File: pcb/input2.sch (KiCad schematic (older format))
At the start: 33 parts, among them U4 PCEngineExpansion, U5 FS7140-01G-XTD, U6 PCM1808PWR, U7 SI5351C-B, U8 74153, Y1 25.000MHz

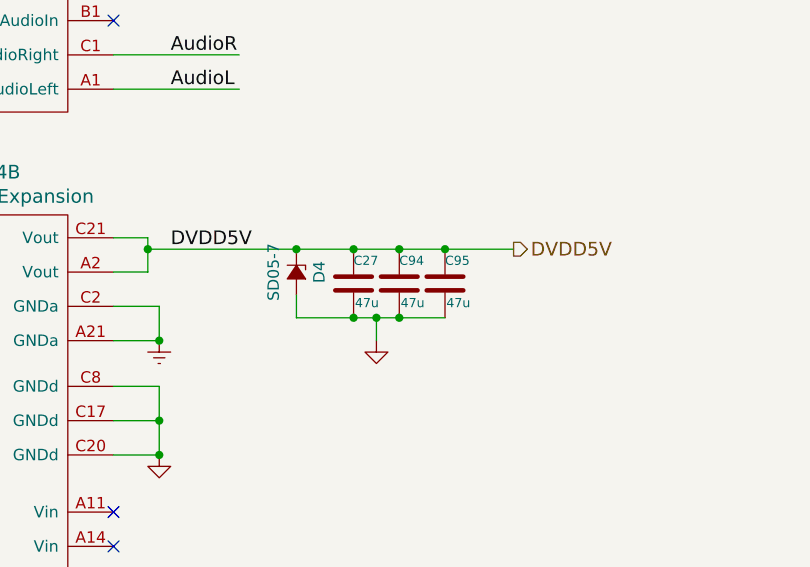
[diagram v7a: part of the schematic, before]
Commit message: Added CDD signal to last open IO pin
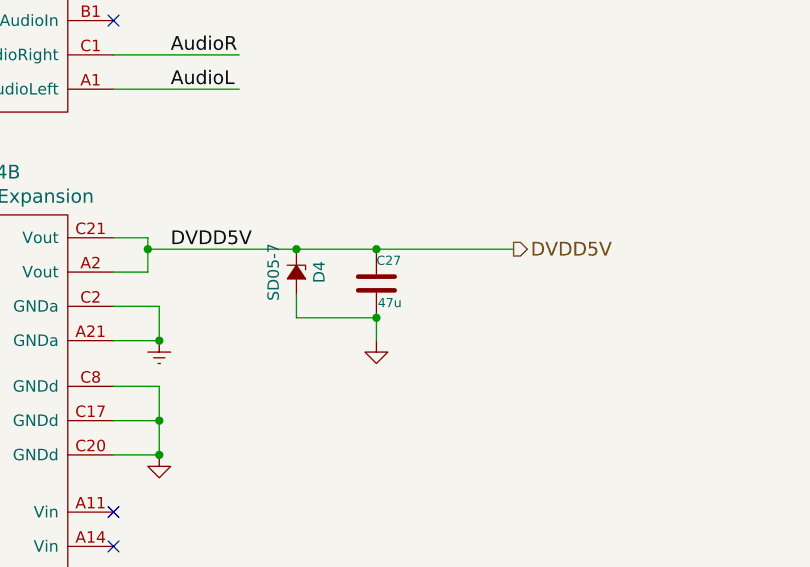
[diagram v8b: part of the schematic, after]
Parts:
- removed C94, C95: 47u, custom_components:SM0603_Capa_libcms, symbol pcehd-rescue:C-Device
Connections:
- wire segments 122 -> 117
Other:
- moved on the sheet: C27
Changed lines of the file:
@@
 Sheet 4 5
 Title "PCEHD"
-Date "2020-01-16"
+Date "2020-01-18"
 Rev "0.1"
 Comp ""
@@
 	1    0    0    -1
 $EndComp
-Wire Wire Line
-	3450 3700 3650 3700
-Wire Wire Line
-	3200 3700 3450 3700
 Text HLabel 4150 3700 2    60   Output ~ 0
 DVDD5V
-Connection ~ 3450 3700
 Connection ~ 3200 3700
 Wire Wire Line
@@
 L pcehd-rescue:C-Device C?
 U 1 1 5ED1A2AA
-P 3450 3850
+P 3550 3850
 AR Path="/5A43CDD8/5ED1A2AA" Ref="C?"  Part="1"
 AR Path="/5ECF4034/5ED1A2AA" Ref="C27"  Part="1"
-F 0 "C27" H 3450 3950 40  0000 L CNN
-F 1 "47u" H 3456 3765 40  0000 L CNN
-F 2 "custom_components:SM0603_Capa_libcms" H 3488 3700 30  0001 C CNN
-F 3 "~" H 3450 3850 60  0000 C CNN
-	1    3450 3850
+F 0 "C27" H 3550 3950 40  0000 L CNN
+F 1 "47u" H 3556 3765 40  0000 L CNN
+F 2 "custom_components:SM0603_Capa_libcms" H 3588 3700 30  0001 C CNN
+F 3 "~" H 3550 3850 60  0000 C CNN
+	1    3550 3850
 	1    0    0    -1
 $EndComp
@@
 	1    0    0    -1
 $EndComp
-$Comp
-L pcehd-rescue:C-Device C?
-U 1 1 5E24D671
-P 3650 3850
-AR Path="/5A43CDD8/5E24D671" Ref="C?"  Part="1"
-AR Path="/5ECF4034/5E24D671" Ref="C94"  Part="1"
-F 0 "C94" H 3650 3950 40  0000 L CNN
-F 1 "47u" H 3656 3765 40  0000 L CNN
-F 2 "custom_components:SM0603_Capa_libcms" H 3688 3700 30  0001 C CNN
-F 3 "~" H 3650 3850 60  0000 C CNN
-	1    3650 3850
-	1    0    0    -1
-$EndComp
-$Comp
-L pcehd-rescue:C-Device C?
-U 1 1 5E251A93
-P 3850 3850
-AR Path="/5A43CDD8/5E251A93" Ref="C?"  Part="1"
-AR Path="/5ECF4034/5E251A93" Ref="C95"  Part="1"
-F 0 "C95" H 3850 3950 40  0000 L CNN
-F 1 "47u" H 3856 3765 40  0000 L CNN
-F 2 "custom_components:SM0603_Capa_libcms" H 3888 3700 30  0001 C CNN
-F 3 "~" H 3850 3850 60  0000 C CNN
-	1    3850 3850
-	1    0    0    -1
-$EndComp
-Wire Wire Line
-	3650 3700 3850 3700
-Connection ~ 3650 3700
-Wire Wire Line
-	3450 4000 3550 4000
-Wire Wire Line
-	3650 4000 3850 4000
-Connection ~ 3450 4000
-Connection ~ 3650 4000
-Wire Wire Line
-	3200 4000 3450 4000
 Wire Wire Line
 	3550 4000 3550 4100
+Connection ~ 3550 3700
+Wire Wire Line
+	3550 3700 4150 3700
 Connection ~ 3550 4000
 Wire Wire Line
-	3550 4000 3650 4000
-Wire Wire Line
-	3850 3700 4150 3700
-Connection ~ 3850 3700
+	3200 3700 3550 3700
+Wire Wire Line
+	3200 4000 3550 4000
 $EndSCHEMATC
